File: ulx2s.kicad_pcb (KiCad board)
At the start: 4 copper layers, 35.6 x 61 mm, 26 parts, among them J1 Conn_01x24, J2 Conn_01x24, J3 Micro_SD_Card_Det, J4 USB_OTG, J5 Conn_01x06, SW1 SW_Push, SW2 SW_Push, SW3 SW_Push, SW4 SW_Push, SW5 SW_Push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

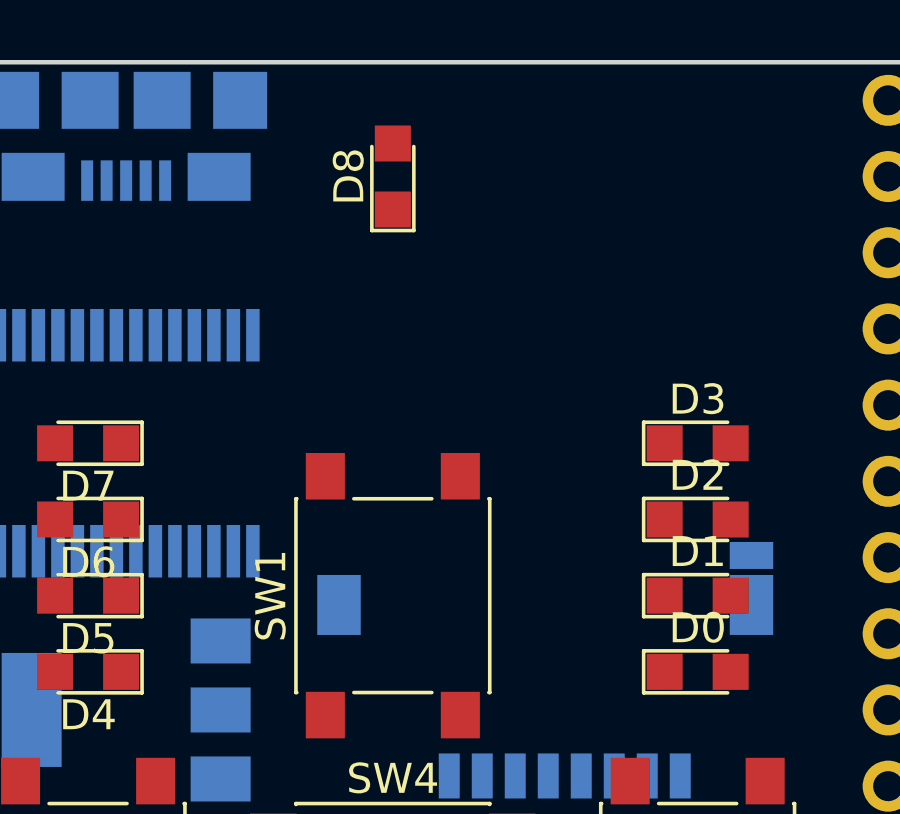
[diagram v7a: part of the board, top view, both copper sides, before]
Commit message: audio jack placed
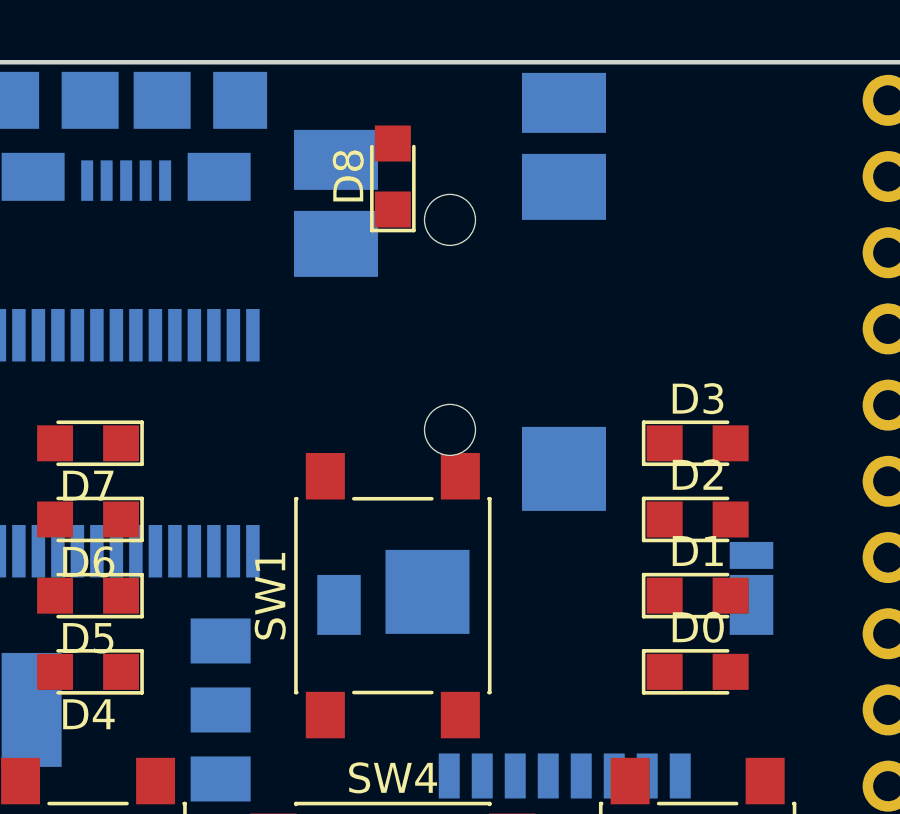
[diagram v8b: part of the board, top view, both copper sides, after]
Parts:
- added J6: Audio-Jack-5, audio-jack:CUI_SJ-43516-SMT, B.Cu at (160.7, 89.5)
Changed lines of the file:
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@@
     (tracks 0)
     (zones 0)
-    (modules 26)
+    (modules 27)
     (nets 13)
   )
@@
     )
   )
+  (module audio-jack:CUI_SJ-43516-SMT (layer B.Cu)
+    (at 160.655 89.535 180)
+    (descr "CUI 6-pin audio jack SMT")
+    (tags "audio jack")
+    (attr smd)
+    (fp_text reference J6 (at -3.560502 -0.28335 270) (layer B.SilkS)
+      (effects (font (size 0.6096 0.6096) (thickness 0.1524)) (justify mirror))
+    )
+    (fp_text value Audio-Jack-5 (at 1.519498 -0.28335 270) (layer B.SilkS)
+      (effects (font (size 1 1) (thickness 0.15)) (justify mirror))
+    )
+    (fp_line (start -2.5 9.1) (end -2.5 8.1) (layer B.SilkS) (width 0.15))
+    (fp_line (start 2.5 9.1) (end -2.5 9.1) (layer B.SilkS) (width 0.15))
+    (fp_line (start 2.5 7.5) (end 2.5 9.1) (layer B.SilkS) (width 0.15))
+    (fp_line (start 3 7.5) (end -2.2 7.5) (layer B.SilkS) (width 0.15))
+    (fp_line (start -3.8 5.4) (end -3.8 5.7) (layer B.SilkS) (width 0.15))
+    (fp_line (start -3.8 1.9) (end -3.8 2.8) (layer B.SilkS) (width 0.15))
+    (fp_line (start -3 1.9) (end -3.8 1.9) (layer B.SilkS) (width 0.15))
+    (fp_line (start -3 -3.7) (end -3 1.9) (layer B.SilkS) (width 0.15))
+    (fp_line (start -3 -7.9) (end -3 -6.9) (layer B.SilkS) (width 0.15))
+    (fp_line (start -3 -7.9) (end 3 -7.9) (layer B.SilkS) (width 0.15))
+    (fp_line (start 3 0.9) (end 3 -7.9) (layer B.SilkS) (width 0.15))
+    (fp_line (start 3 3.8) (end 3 3.5) (layer B.SilkS) (width 0.15))
+    (fp_line (start 3 7.5) (end 3 6.2) (layer B.SilkS) (width 0.15))
+    (pad 1 smd rect (at -3.8 6.9 270) (size 2 2.8) (layers B.Cu B.Paste B.Mask))
+    (pad 4 smd rect (at -3.8 4.1 270) (size 2.2 2.8) (layers B.Cu B.Paste B.Mask))
+    (pad 2 smd rect (at -3.8 -5.3 270) (size 2.8 2.8) (layers B.Cu B.Paste B.Mask))
+    (pad 5 smd rect (at 0.75 -9.4 270) (size 2.8 2.8) (layers B.Cu B.Paste B.Mask))
+    (pad 3 smd rect (at 3.8 2.2 270) (size 2.2 2.8) (layers B.Cu B.Paste B.Mask))
+    (pad 6 smd rect (at 3.8 5 270) (size 2 2.8) (layers B.Cu B.Paste B.Mask))
+    (pad "" np_thru_hole circle (at 0 3 270) (size 1.7 1.7) (drill 1.7) (layers *.Cu *.Mask B.SilkS)
+      (clearance 0.4))
+    (pad "" np_thru_hole circle (at 0 -4 270) (size 1.7 1.7) (drill 1.7) (layers *.Cu *.Mask B.SilkS)
+      (clearance 0.4))
+  )
   (gr_line (start 140.97 81.28) (end 140.97 142.24) (layer Edge.Cuts) (width 0.15))
